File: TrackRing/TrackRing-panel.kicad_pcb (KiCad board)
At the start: 2 copper layers, 68 x 83 mm, 225 parts, among them J1 Conn_01x04, U1 TLV493D-A1B6

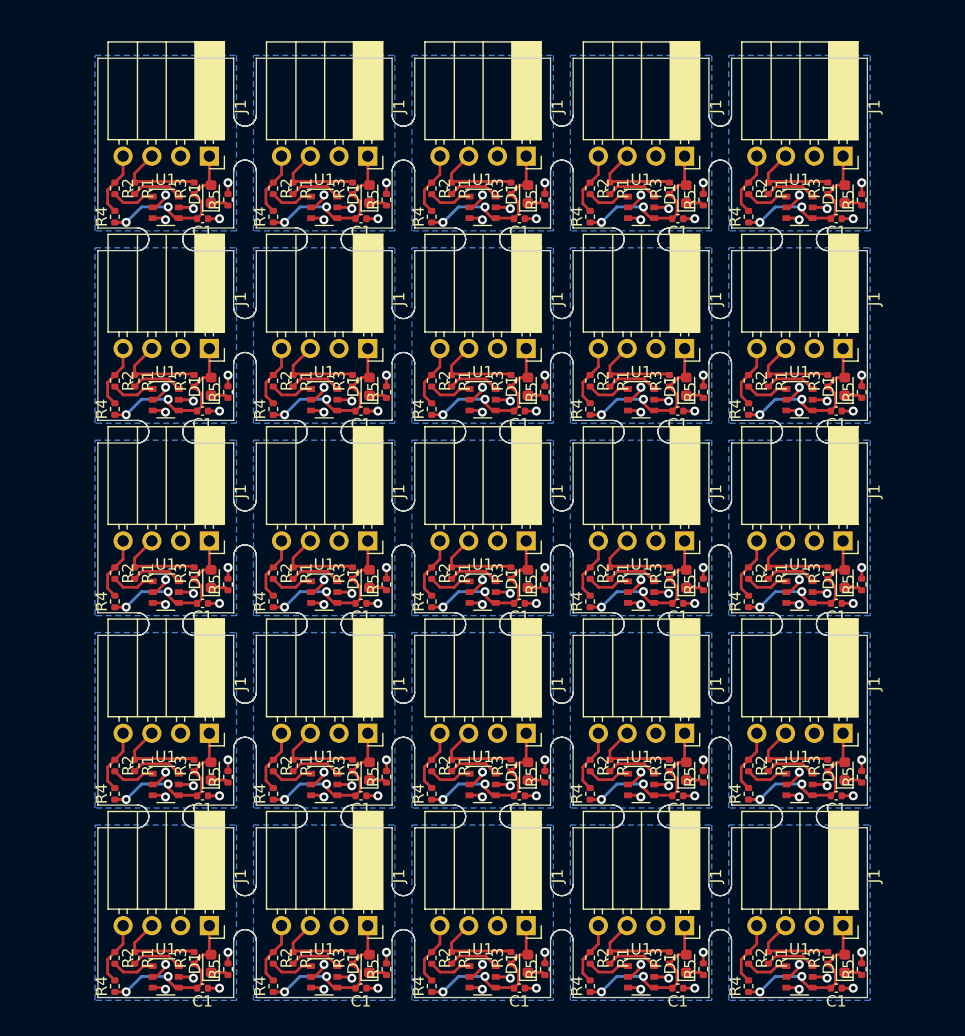
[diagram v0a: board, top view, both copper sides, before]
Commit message: Resolved various production and testing issues
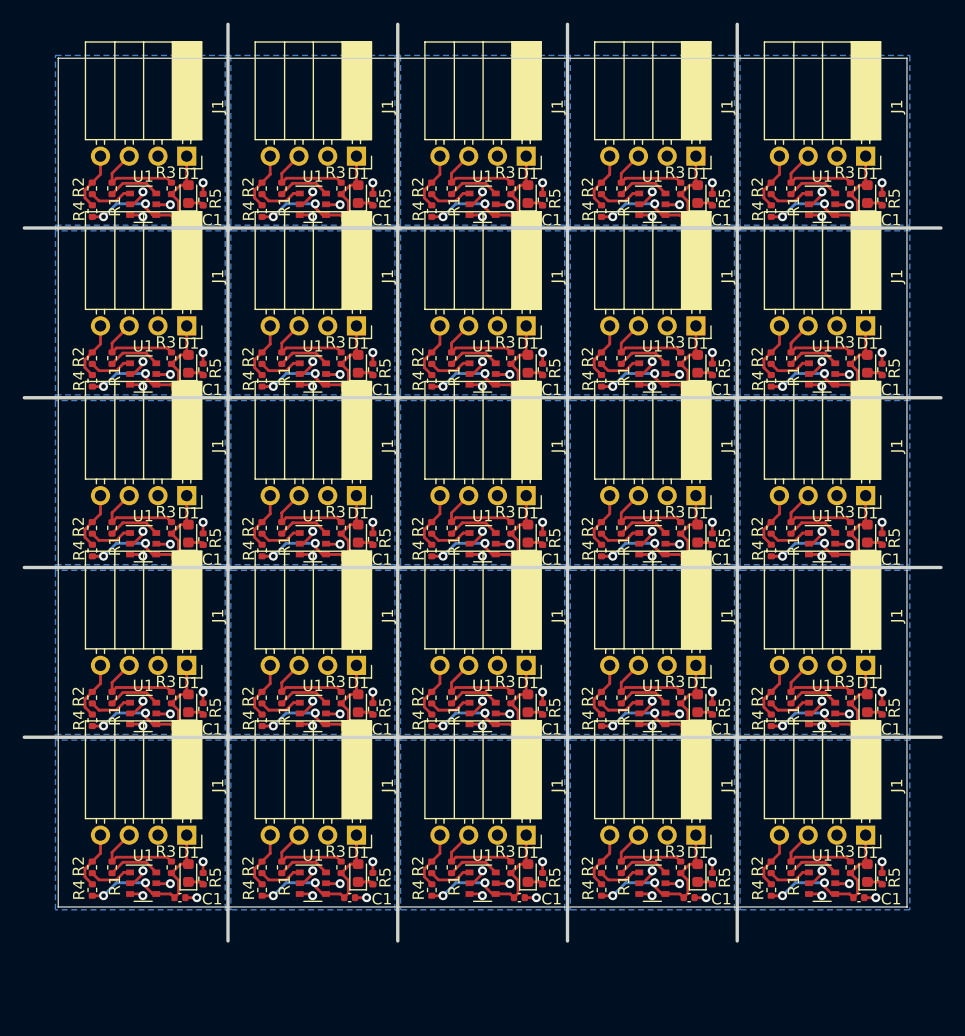
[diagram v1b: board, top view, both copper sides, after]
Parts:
- removed the C1 at (151.8, 102.2)
- removed the C1 at (179.8, 85.2)
- removed the C1 at (179.8, 34.2)
- removed the C1 at (165.8, 85.2)
- removed the C1 at (151.8, 51.2)
- removed the C1 at (123.8, 68.2)
- removed the C1 at (165.8, 102.2)
- removed the C1 at (179.8, 102.2)
- removed the C1 at (123.8, 51.2)
- removed the C1 at (151.8, 85.2)
- removed the C1 at (137.8, 51.2)
- removed the C1 at (123.8, 85.2)
- removed the C1 at (165.8, 68.2)
- removed the C1 at (165.8, 34.2)
- removed the C1 at (151.8, 34.2)
- removed the C1 at (179.8, 51.2)
- removed the C1 at (165.8, 51.2)
- removed the C1 at (179.8, 68.2)
- removed the C1 at (151.8, 68.2)
- removed the C1 at (137.8, 85.2)
- removed the C1 at (137.8, 68.2)
- removed the C1 at (137.8, 34.2)
- removed the C1 at (123.8, 102.2)
- removed the C1 at (137.8, 102.2)
- removed the D1 at (166.5, 100.0)
- removed the D1 at (180.5, 49.0)
- removed the D1 at (138.5, 49.0)
- removed the D1 at (180.5, 83.0)
- removed the D1 at (152.5, 100.0)
- removed the D1 at (166.5, 83.0)
- removed the D1 at (124.5, 66.0)
- removed the D1 at (124.5, 100.0)
- removed the D1 at (180.5, 66.0)
- removed the D1 at (138.5, 32.0)
- removed the D1 at (166.5, 49.0)
- removed the D1 at (124.5, 83.0)
- removed the D1 at (166.5, 32.0)
- removed the D1 at (138.5, 83.0)
- removed the D1 at (180.5, 32.0)
- removed the D1 at (138.5, 100.0)
- removed the D1 at (152.5, 83.0)
- removed the D1 at (138.5, 66.0)
- removed the D1 at (152.5, 66.0)
- removed the D1 at (124.5, 32.0)
- removed the D1 at (166.5, 66.0)
- removed the D1 at (152.5, 49.0)
- removed the D1 at (180.5, 100.0)
- removed the J1 at (152.3, 62.6)
- removed the J1 at (152.3, 45.6)
- removed the J1 at (124.3, 45.6)
- removed the J1 at (180.3, 45.6)
- removed the J1 at (124.3, 96.7)
- removed the J1 at (124.3, 79.7)
- removed the J1 at (138.3, 62.6)
- removed the J1 at (138.3, 96.7)
- removed the J1 at (152.3, 96.7)
- removed the J1 at (180.3, 96.7)
- removed the J1 at (124.3, 28.6)
- removed the J1 at (180.3, 79.7)
- removed the J1 at (152.3, 79.7)
- removed the J1 at (180.3, 28.6)
- removed the J1 at (166.3, 79.7)
- removed the J1 at (166.3, 96.7)
- removed the J1 at (138.3, 79.7)
- removed the J1 at (166.3, 28.6)
- removed the J1 at (180.3, 62.6)
- removed the J1 at (166.3, 45.6)
- removed the J1 at (138.3, 45.6)
- removed the J1 at (124.3, 62.6)
- removed the J1 at (166.3, 62.6)
- removed the R1 at (117.8, 99.5)
- removed the R1 at (117.8, 65.5)
- removed the R1 at (173.8, 48.5)
- removed the R1 at (131.8, 48.5)
- removed the R1 at (145.8, 48.5)
- removed the R1 at (145.8, 99.5)
- removed the R1 at (145.8, 82.5)
- removed the R1 at (131.8, 99.5)
- removed the R1 at (131.8, 65.5)
- removed the R1 at (173.8, 31.5)
- removed the R1 at (117.8, 82.5)
- removed the R1 at (131.8, 31.5)
- removed the R1 at (117.8, 48.5)
- removed the R1 at (159.8, 48.5)
- removed the R1 at (159.8, 65.5)
- removed the R1 at (173.8, 82.5)
- removed the R1 at (173.8, 99.5)
- removed the R1 at (145.8, 65.5)
- removed the R1 at (159.8, 82.5)
- removed the R1 at (159.8, 99.5)
- removed the R1 at (131.8, 82.5)
- removed the R1 at (117.8, 31.5)
- removed the R1 at (173.8, 65.5)
- removed the R2 at (172.0, 65.5)
- removed the R2 at (116.0, 48.5)
- removed the R2 at (172.0, 99.5)
- removed the R2 at (130.0, 65.5)
- removed the R2 at (116.0, 65.5)
- removed the R2 at (144.0, 48.5)
- removed the R2 at (144.0, 82.5)
- removed the R2 at (172.0, 48.5)
- removed the R2 at (130.0, 31.5)
- removed the R2 at (130.0, 82.5)
- removed the R2 at (158.0, 99.5)
- removed the R2 at (158.0, 31.5)
- removed the R2 at (172.0, 82.5)
- removed the R2 at (144.0, 99.5)
- removed the R2 at (130.0, 99.5)
- removed the R2 at (130.0, 48.5)
- removed the R2 at (158.0, 48.5)
- removed the R2 at (158.0, 65.5)
- removed the R2 at (116.0, 99.5)
- removed the R2 at (158.0, 82.5)
- removed the R2 at (144.0, 65.5)
- removed the R2 at (116.0, 82.5)
- removed the R2 at (172.0, 31.5)
- removed the R3 at (151.0, 48.5)
- removed the R3 at (151.0, 82.5)
- removed the R3 at (123.0, 48.5)
- removed the R3 at (151.0, 99.5)
- removed the R3 at (137.0, 65.5)
- removed the R3 at (137.0, 48.5)
- removed the R3 at (137.0, 99.5)
- removed the R3 at (123.0, 31.5)
- removed the R3 at (165.0, 65.5)
- removed the R3 at (165.0, 82.5)
- removed the R3 at (123.0, 99.5)
- removed the R3 at (165.0, 48.5)
- removed the R3 at (179.0, 48.5)
- removed the R3 at (179.0, 65.5)
- removed the R3 at (165.0, 99.5)
- removed the R3 at (137.0, 82.5)
- removed the R3 at (179.0, 99.5)
- removed the R3 at (123.0, 65.5)
- removed the R3 at (151.0, 65.5)
- removed the R3 at (137.0, 31.5)
- removed the R3 at (179.0, 82.5)
- removed the R3 at (123.0, 82.5)
- removed the R3 at (165.0, 31.5)
- removed the R4 at (144.0, 68.0)
- removed the R4 at (172.0, 102.0)
- removed the R4 at (130.0, 102.0)
- removed the R4 at (172.0, 34.0)
- removed the R4 at (130.0, 51.0)
- removed the R4 at (158.0, 51.0)
- removed the R4 at (116.0, 51.0)
- removed the R4 at (158.0, 102.0)
- removed the R4 at (116.0, 102.0)
- removed the R4 at (144.0, 85.0)
- removed the R4 at (144.0, 51.0)
- removed the R4 at (172.0, 68.0)
- removed the R4 at (144.0, 102.0)
- removed the R4 at (158.0, 68.0)
- removed the R4 at (144.0, 34.0)
- removed the R4 at (158.0, 34.0)
- removed the R4 at (158.0, 85.0)
- removed the R4 at (116.0, 34.0)
- removed the R4 at (130.0, 68.0)
- removed the R4 at (116.0, 85.0)
- removed the R4 at (116.0, 68.0)
- removed the R4 at (172.0, 51.0)
- removed the R4 at (172.0, 85.0)
- removed the R4 at (130.0, 85.0)
- removed the R5 at (154.0, 66.5)
- removed the R5 at (140.0, 83.5)
- removed the R5 at (126.0, 83.5)
- removed the R5 at (182.0, 32.5)
- removed the R5 at (154.0, 100.5)
- removed the R5 at (182.0, 49.5)
- removed the R5 at (154.0, 32.5)
- removed the R5 at (168.0, 66.5)
- removed the R5 at (154.0, 49.5)
- removed the R5 at (126.0, 100.5)
- removed the R5 at (182.0, 83.5)
- removed the R5 at (168.0, 49.5)
- removed the R5 at (154.0, 83.5)
- removed the R5 at (140.0, 49.5)
- removed the R5 at (126.0, 49.5)
- removed the R5 at (126.0, 66.5)
- removed the R5 at (140.0, 100.5)
- removed the R5 at (182.0, 100.5)
- removed the R5 at (126.0, 32.5)
- removed the R5 at (168.0, 100.5)
- removed the R5 at (168.0, 83.5)
- removed the R5 at (168.0, 32.5)
- removed the R5 at (182.0, 66.5)
- removed the R5 at (140.0, 66.5)
- removed the U1 at (162.5, 50.2)
- removed the U1 at (176.5, 67.2)
- removed the U1 at (148.5, 84.2)
- removed the U1 at (176.5, 101.2)
- removed the U1 at (120.5, 84.2)
- removed the U1 at (176.5, 50.2)
- removed the U1 at (120.5, 33.2)
- removed the U1 at (120.5, 50.2)
- removed the U1 at (134.5, 50.2)
- removed the U1 at (176.5, 84.2)
- removed the U1 at (162.5, 67.2)
- removed the U1 at (134.5, 67.2)
- removed the U1 at (148.5, 50.2)
- removed the U1 at (134.5, 84.2)
- removed the U1 at (176.5, 33.2)
- removed the U1 at (134.5, 101.2)
- removed the U1 at (148.5, 33.2)
- removed the U1 at (148.5, 101.2)
- removed the U1 at (120.5, 67.2)
- removed the U1 at (148.5, 67.2)
- removed the U1 at (162.5, 33.2)
- removed the U1 at (134.5, 33.2)
- removed the U1 at (120.5, 101.2)
- removed the U1 at (162.5, 101.2)
- added C1: 0.1uF, Capacitor_SMD:C_0402_1005Metric, F.Cu at (136.8, 94.2)
- added C1: 0.1uF, Capacitor_SMD:C_0402_1005Metric, F.Cu at (166.8, 79.2)
- added C1: 0.1uF, Capacitor_SMD:C_0402_1005Metric, F.Cu at (136.8, 64.2)
- added C1: 0.1uF, Capacitor_SMD:C_0402_1005Metric, F.Cu at (136.8, 79.2)
- added C1: 0.1uF, Capacitor_SMD:C_0402_1005Metric, F.Cu at (121.8, 79.2)
- added C1: 0.1uF, Capacitor_SMD:C_0402_1005Metric, F.Cu at (166.8, 94.2)
- added C1: 0.1uF, Capacitor_SMD:C_0402_1005Metric, F.Cu at (151.8, 94.2)
- added C1: 0.1uF, Capacitor_SMD:C_0402_1005Metric, F.Cu at (121.8, 49.2)
- added C1: 0.1uF, Capacitor_SMD:C_0402_1005Metric, F.Cu at (166.8, 49.2)
- added C1: 0.1uF, Capacitor_SMD:C_0402_1005Metric, F.Cu at (121.8, 34.2)
- added C1: 0.1uF, Capacitor_SMD:C_0402_1005Metric, F.Cu at (181.8, 94.2)
- added C1: 0.1uF, Capacitor_SMD:C_0402_1005Metric, F.Cu at (151.8, 64.2)
- added C1: 0.1uF, Capacitor_SMD:C_0402_1005Metric, F.Cu at (136.8, 34.2)
- added C1: 0.1uF, Capacitor_SMD:C_0402_1005Metric, F.Cu at (121.8, 94.2)
- added C1: 0.1uF, Capacitor_SMD:C_0402_1005Metric, F.Cu at (181.8, 49.2)
- added C1: 0.1uF, Capacitor_SMD:C_0402_1005Metric, F.Cu at (166.8, 34.2)
- added C1: 0.1uF, Capacitor_SMD:C_0402_1005Metric, F.Cu at (181.8, 34.2)
- added C1: 0.1uF, Capacitor_SMD:C_0402_1005Metric, F.Cu at (166.8, 64.2)
- added C1: 0.1uF, Capacitor_SMD:C_0402_1005Metric, F.Cu at (181.8, 79.2)
- added C1: 0.1uF, Capacitor_SMD:C_0402_1005Metric, F.Cu at (151.8, 79.2)
- added C1: 0.1uF, Capacitor_SMD:C_0402_1005Metric, F.Cu at (121.8, 64.2)
- added C1: 0.1uF, Capacitor_SMD:C_0402_1005Metric, F.Cu at (151.8, 49.2)
- added C1: 0.1uF, Capacitor_SMD:C_0402_1005Metric, F.Cu at (181.8, 64.2)
- added C1: 0.1uF, Capacitor_SMD:C_0402_1005Metric, F.Cu at (136.8, 49.2)
- added D1: LED, LED_SMD:LED_0603_1608Metric, F.Cu at (122.5, 77.0)
- added D1: LED, LED_SMD:LED_0603_1608Metric, F.Cu at (137.5, 77.0)
- added D1: LED, LED_SMD:LED_0603_1608Metric, F.Cu at (167.5, 47.0)
- added D1: LED, LED_SMD:LED_0603_1608Metric, F.Cu at (122.5, 62.0)
- added D1: LED, LED_SMD:LED_0603_1608Metric, F.Cu at (152.5, 77.0)
- added D1: LED, LED_SMD:LED_0603_1608Metric, F.Cu at (137.5, 32.0)
- added D1: LED, LED_SMD:LED_0603_1608Metric, F.Cu at (167.5, 62.0)
- added D1: LED, LED_SMD:LED_0603_1608Metric, F.Cu at (152.5, 62.0)
- added D1: LED, LED_SMD:LED_0603_1608Metric, F.Cu at (182.5, 32.0)
- added D1: LED, LED_SMD:LED_0603_1608Metric, F.Cu at (152.5, 92.0)
- added D1: LED, LED_SMD:LED_0603_1608Metric, F.Cu at (137.5, 47.0)
- added D1: LED, LED_SMD:LED_0603_1608Metric, F.Cu at (182.5, 77.0)
- added D1: LED, LED_SMD:LED_0603_1608Metric, F.Cu at (137.5, 92.0)
- added D1: LED, LED_SMD:LED_0603_1608Metric, F.Cu at (122.5, 32.0)
- added D1: LED, LED_SMD:LED_0603_1608Metric, F.Cu at (182.5, 62.0)
- added D1: LED, LED_SMD:LED_0603_1608Metric, F.Cu at (182.5, 92.0)
- added D1: LED, LED_SMD:LED_0603_1608Metric, F.Cu at (137.5, 62.0)
- added D1: LED, LED_SMD:LED_0603_1608Metric, F.Cu at (152.5, 47.0)
- added D1: LED, LED_SMD:LED_0603_1608Metric, F.Cu at (167.5, 77.0)
- added D1: LED, LED_SMD:LED_0603_1608Metric, F.Cu at (167.5, 92.0)
- added D1: LED, LED_SMD:LED_0603_1608Metric, F.Cu at (167.5, 32.0)
- added D1: LED, LED_SMD:LED_0603_1608Metric, F.Cu at (122.5, 47.0)
- added D1: LED, LED_SMD:LED_0603_1608Metric, F.Cu at (182.5, 47.0)
- added J1: Conn_01x04, Connector_PinSocket_2.54mm:PinSocket_1x04_P2.54mm_Horizontal, F.Cu at (152.3, 43.6)
- added J1: Conn_01x04, Connector_PinSocket_2.54mm:PinSocket_1x04_P2.54mm_Horizontal, F.Cu at (167.3, 88.7)
- added J1: Conn_01x04, Connector_PinSocket_2.54mm:PinSocket_1x04_P2.54mm_Horizontal, F.Cu at (137.3, 43.6)
- added J1: Conn_01x04, Connector_PinSocket_2.54mm:PinSocket_1x04_P2.54mm_Horizontal, F.Cu at (167.3, 28.6)
- added J1: Conn_01x04, Connector_PinSocket_2.54mm:PinSocket_1x04_P2.54mm_Horizontal, F.Cu at (182.3, 88.7)
- added J1: Conn_01x04, Connector_PinSocket_2.54mm:PinSocket_1x04_P2.54mm_Horizontal, F.Cu at (152.3, 58.6)
- added J1: Conn_01x04, Connector_PinSocket_2.54mm:PinSocket_1x04_P2.54mm_Horizontal, F.Cu at (122.3, 43.6)
- added J1: Conn_01x04, Connector_PinSocket_2.54mm:PinSocket_1x04_P2.54mm_Horizontal, F.Cu at (122.3, 88.7)
- added J1: Conn_01x04, Connector_PinSocket_2.54mm:PinSocket_1x04_P2.54mm_Horizontal, F.Cu at (152.3, 88.7)
- added J1: Conn_01x04, Connector_PinSocket_2.54mm:PinSocket_1x04_P2.54mm_Horizontal, F.Cu at (137.3, 88.7)
- added J1: Conn_01x04, Connector_PinSocket_2.54mm:PinSocket_1x04_P2.54mm_Horizontal, F.Cu at (137.3, 73.7)
- added J1: Conn_01x04, Connector_PinSocket_2.54mm:PinSocket_1x04_P2.54mm_Horizontal, F.Cu at (122.3, 28.6)
- added J1: Conn_01x04, Connector_PinSocket_2.54mm:PinSocket_1x04_P2.54mm_Horizontal, F.Cu at (167.3, 43.6)
- added J1: Conn_01x04, Connector_PinSocket_2.54mm:PinSocket_1x04_P2.54mm_Horizontal, F.Cu at (182.3, 73.7)
- added J1: Conn_01x04, Connector_PinSocket_2.54mm:PinSocket_1x04_P2.54mm_Horizontal, F.Cu at (167.3, 58.6)
- added J1: Conn_01x04, Connector_PinSocket_2.54mm:PinSocket_1x04_P2.54mm_Horizontal, F.Cu at (122.3, 58.6)
- added J1: Conn_01x04, Connector_PinSocket_2.54mm:PinSocket_1x04_P2.54mm_Horizontal, F.Cu at (182.3, 28.6)
- added J1: Conn_01x04, Connector_PinSocket_2.54mm:PinSocket_1x04_P2.54mm_Horizontal, F.Cu at (182.3, 43.6)
- added J1: Conn_01x04, Connector_PinSocket_2.54mm:PinSocket_1x04_P2.54mm_Horizontal, F.Cu at (152.3, 73.7)
- added J1: Conn_01x04, Connector_PinSocket_2.54mm:PinSocket_1x04_P2.54mm_Horizontal, F.Cu at (182.3, 58.6)
- added J1: Conn_01x04, Connector_PinSocket_2.54mm:PinSocket_1x04_P2.54mm_Horizontal, F.Cu at (122.3, 73.7)
- added J1: Conn_01x04, Connector_PinSocket_2.54mm:PinSocket_1x04_P2.54mm_Horizontal, F.Cu at (137.3, 58.6)
- added J1: Conn_01x04, Connector_PinSocket_2.54mm:PinSocket_1x04_P2.54mm_Horizontal, F.Cu at (167.3, 73.7)
- added R1: 100, Resistor_SMD:R_0402_1005Metric, F.Cu at (115.8, 91.5)
- added R1: 100, Resistor_SMD:R_0402_1005Metric, F.Cu at (160.8, 46.5)
- added R1: 100, Resistor_SMD:R_0402_1005Metric, F.Cu at (145.8, 46.5)
- added R1: 100, Resistor_SMD:R_0402_1005Metric, F.Cu at (115.8, 31.5)
- added R1: 100, Resistor_SMD:R_0402_1005Metric, F.Cu at (130.8, 76.5)
- added R1: 100, Resistor_SMD:R_0402_1005Metric, F.Cu at (160.8, 91.5)
- added R1: 100, Resistor_SMD:R_0402_1005Metric, F.Cu at (115.8, 46.5)
- added R1: 100, Resistor_SMD:R_0402_1005Metric, F.Cu at (175.8, 91.5)
- added R1: 100, Resistor_SMD:R_0402_1005Metric, F.Cu at (130.8, 46.5)
- added R1: 100, Resistor_SMD:R_0402_1005Metric, F.Cu at (175.8, 31.5)
- added R1: 100, Resistor_SMD:R_0402_1005Metric, F.Cu at (115.8, 61.5)
- added R1: 100, Resistor_SMD:R_0402_1005Metric, F.Cu at (115.8, 76.5)
- added R1: 100, Resistor_SMD:R_0402_1005Metric, F.Cu at (160.8, 61.5)
- added R1: 100, Resistor_SMD:R_0402_1005Metric, F.Cu at (160.8, 76.5)
- added R1: 100, Resistor_SMD:R_0402_1005Metric, F.Cu at (130.8, 31.5)
- added R1: 100, Resistor_SMD:R_0402_1005Metric, F.Cu at (145.8, 76.5)
- added R1: 100, Resistor_SMD:R_0402_1005Metric, F.Cu at (175.8, 46.5)
- added R1: 100, Resistor_SMD:R_0402_1005Metric, F.Cu at (130.8, 61.5)
- added R1: 100, Resistor_SMD:R_0402_1005Metric, F.Cu at (175.8, 76.5)
- added R1: 100, Resistor_SMD:R_0402_1005Metric, F.Cu at (160.8, 31.5)
- added R1: 100, Resistor_SMD:R_0402_1005Metric, F.Cu at (145.8, 91.5)
- added R1: 100, Resistor_SMD:R_0402_1005Metric, F.Cu at (175.8, 61.5)
- added R1: 100, Resistor_SMD:R_0402_1005Metric, F.Cu at (130.8, 91.5)
- added R2: 100, Resistor_SMD:R_0402_1005Metric, F.Cu at (174.0, 61.5)
- added R2: 100, Resistor_SMD:R_0402_1005Metric, F.Cu at (129.0, 91.5)
- added R2: 100, Resistor_SMD:R_0402_1005Metric, F.Cu at (174.0, 91.5)
- added R2: 100, Resistor_SMD:R_0402_1005Metric, F.Cu at (114.0, 76.5)
- added R2: 100, Resistor_SMD:R_0402_1005Metric, F.Cu at (174.0, 76.5)
- added R2: 100, Resistor_SMD:R_0402_1005Metric, F.Cu at (129.0, 76.5)
- added R2: 100, Resistor_SMD:R_0402_1005Metric, F.Cu at (159.0, 46.5)
- added R2: 100, Resistor_SMD:R_0402_1005Metric, F.Cu at (144.0, 61.5)
- added R2: 100, Resistor_SMD:R_0402_1005Metric, F.Cu at (114.0, 61.5)
- added R2: 100, Resistor_SMD:R_0402_1005Metric, F.Cu at (129.0, 61.5)
- added R2: 100, Resistor_SMD:R_0402_1005Metric, F.Cu at (159.0, 76.5)
- added R2: 100, Resistor_SMD:R_0402_1005Metric, F.Cu at (144.0, 46.5)
- added R2: 100, Resistor_SMD:R_0402_1005Metric, F.Cu at (144.0, 76.5)
- added R2: 100, Resistor_SMD:R_0402_1005Metric, F.Cu at (159.0, 31.5)
- added R2: 100, Resistor_SMD:R_0402_1005Metric, F.Cu at (159.0, 91.5)
- added R2: 100, Resistor_SMD:R_0402_1005Metric, F.Cu at (159.0, 61.5)
- added R2: 100, Resistor_SMD:R_0402_1005Metric, F.Cu at (144.0, 91.5)
- added R2: 100, Resistor_SMD:R_0402_1005Metric, F.Cu at (114.0, 31.5)
- added R2: 100, Resistor_SMD:R_0402_1005Metric, F.Cu at (114.0, 91.5)
- added R2: 100, Resistor_SMD:R_0402_1005Metric, F.Cu at (129.0, 31.5)
- added R2: 100, Resistor_SMD:R_0402_1005Metric, F.Cu at (129.0, 46.5)
- added R2: 100, Resistor_SMD:R_0402_1005Metric, F.Cu at (174.0, 31.5)
- added R2: 100, Resistor_SMD:R_0402_1005Metric, F.Cu at (174.0, 46.5)
- added R3: 1.2K, Resistor_SMD:R_0402_1005Metric, F.Cu at (181.0, 76.5)
- added R3: 1.2K, Resistor_SMD:R_0402_1005Metric, F.Cu at (151.0, 46.5)
- added R3: 1.2K, Resistor_SMD:R_0402_1005Metric, F.Cu at (121.0, 91.5)
- added R3: 1.2K, Resistor_SMD:R_0402_1005Metric, F.Cu at (181.0, 61.5)
- added R3: 1.2K, Resistor_SMD:R_0402_1005Metric, F.Cu at (166.0, 31.5)
- added R3: 1.2K, Resistor_SMD:R_0402_1005Metric, F.Cu at (121.0, 46.5)
- added R3: 1.2K, Resistor_SMD:R_0402_1005Metric, F.Cu at (181.0, 91.5)
- added R3: 1.2K, Resistor_SMD:R_0402_1005Metric, F.Cu at (121.0, 31.5)
- added R3: 1.2K, Resistor_SMD:R_0402_1005Metric, F.Cu at (136.0, 76.5)
- added R3: 1.2K, Resistor_SMD:R_0402_1005Metric, F.Cu at (121.0, 61.5)
- added R3: 1.2K, Resistor_SMD:R_0402_1005Metric, F.Cu at (151.0, 91.5)
- added R3: 1.2K, Resistor_SMD:R_0402_1005Metric, F.Cu at (136.0, 31.5)
- added R3: 1.2K, Resistor_SMD:R_0402_1005Metric, F.Cu at (121.0, 76.5)
- added R3: 1.2K, Resistor_SMD:R_0402_1005Metric, F.Cu at (181.0, 46.5)
- added R3: 1.2K, Resistor_SMD:R_0402_1005Metric, F.Cu at (151.0, 76.5)
- added R3: 1.2K, Resistor_SMD:R_0402_1005Metric, F.Cu at (136.0, 61.5)
- added R3: 1.2K, Resistor_SMD:R_0402_1005Metric, F.Cu at (151.0, 61.5)
- added R3: 1.2K, Resistor_SMD:R_0402_1005Metric, F.Cu at (166.0, 61.5)
- added R3: 1.2K, Resistor_SMD:R_0402_1005Metric, F.Cu at (166.0, 76.5)
- added R3: 1.2K, Resistor_SMD:R_0402_1005Metric, F.Cu at (166.0, 91.5)
- added R3: 1.2K, Resistor_SMD:R_0402_1005Metric, F.Cu at (136.0, 91.5)
- added R3: 1.2K, Resistor_SMD:R_0402_1005Metric, F.Cu at (166.0, 46.5)
- added R3: 1.2K, Resistor_SMD:R_0402_1005Metric, F.Cu at (136.0, 46.5)
- added R4: 1.2K, Resistor_SMD:R_0402_1005Metric, F.Cu at (129.0, 78.5)
- added R4: 1.2K, Resistor_SMD:R_0402_1005Metric, F.Cu at (159.0, 93.5)
- added R4: 1.2K, Resistor_SMD:R_0402_1005Metric, F.Cu at (174.0, 63.5)
- added R4: 1.2K, Resistor_SMD:R_0402_1005Metric, F.Cu at (129.0, 33.5)
- added R4: 1.2K, Resistor_SMD:R_0402_1005Metric, F.Cu at (144.0, 93.5)
- added R4: 1.2K, Resistor_SMD:R_0402_1005Metric, F.Cu at (159.0, 63.5)
- added R4: 1.2K, Resistor_SMD:R_0402_1005Metric, F.Cu at (129.0, 93.5)
- added R4: 1.2K, Resistor_SMD:R_0402_1005Metric, F.Cu at (114.0, 33.5)
- added R4: 1.2K, Resistor_SMD:R_0402_1005Metric, F.Cu at (114.0, 93.5)
- added R4: 1.2K, Resistor_SMD:R_0402_1005Metric, F.Cu at (144.0, 33.5)
- added R4: 1.2K, Resistor_SMD:R_0402_1005Metric, F.Cu at (114.0, 63.5)
- added R4: 1.2K, Resistor_SMD:R_0402_1005Metric, F.Cu at (159.0, 48.5)
- added R4: 1.2K, Resistor_SMD:R_0402_1005Metric, F.Cu at (129.0, 63.5)
- added R4: 1.2K, Resistor_SMD:R_0402_1005Metric, F.Cu at (144.0, 63.5)
- added R4: 1.2K, Resistor_SMD:R_0402_1005Metric, F.Cu at (174.0, 78.5)
- added R4: 1.2K, Resistor_SMD:R_0402_1005Metric, F.Cu at (174.0, 33.5)
- added R4: 1.2K, Resistor_SMD:R_0402_1005Metric, F.Cu at (114.0, 48.5)
- added R4: 1.2K, Resistor_SMD:R_0402_1005Metric, F.Cu at (174.0, 93.5)
- added R4: 1.2K, Resistor_SMD:R_0402_1005Metric, F.Cu at (114.0, 78.5)
- added R4: 1.2K, Resistor_SMD:R_0402_1005Metric, F.Cu at (129.0, 48.5)
- added R4: 1.2K, Resistor_SMD:R_0402_1005Metric, F.Cu at (144.0, 48.5)
- added R4: 1.2K, Resistor_SMD:R_0402_1005Metric, F.Cu at (174.0, 48.5)
- added R4: 1.2K, Resistor_SMD:R_0402_1005Metric, F.Cu at (144.0, 78.5)
- added R4: 1.2K, Resistor_SMD:R_0402_1005Metric, F.Cu at (159.0, 78.5)
- added R5: 500, Resistor_SMD:R_0402_1005Metric, F.Cu at (123.8, 92.5)
- added R5: 500, Resistor_SMD:R_0402_1005Metric, F.Cu at (183.8, 47.5)
- added R5: 500, Resistor_SMD:R_0402_1005Metric, F.Cu at (153.8, 47.5)
- added R5: 500, Resistor_SMD:R_0402_1005Metric, F.Cu at (138.8, 77.5)
- added R5: 500, Resistor_SMD:R_0402_1005Metric, F.Cu at (153.8, 77.5)
- added R5: 500, Resistor_SMD:R_0402_1005Metric, F.Cu at (183.8, 62.5)
- added R5: 500, Resistor_SMD:R_0402_1005Metric, F.Cu at (183.8, 32.5)
- added R5: 500, Resistor_SMD:R_0402_1005Metric, F.Cu at (168.8, 92.5)
- added R5: 500, Resistor_SMD:R_0402_1005Metric, F.Cu at (123.8, 32.5)
- added R5: 500, Resistor_SMD:R_0402_1005Metric, F.Cu at (138.8, 92.5)
- added R5: 500, Resistor_SMD:R_0402_1005Metric, F.Cu at (123.8, 47.5)
- added R5: 500, Resistor_SMD:R_0402_1005Metric, F.Cu at (153.8, 32.5)
- added R5: 500, Resistor_SMD:R_0402_1005Metric, F.Cu at (183.8, 92.5)
- added R5: 500, Resistor_SMD:R_0402_1005Metric, F.Cu at (168.8, 32.5)
- added R5: 500, Resistor_SMD:R_0402_1005Metric, F.Cu at (123.8, 77.5)
- added R5: 500, Resistor_SMD:R_0402_1005Metric, F.Cu at (153.8, 92.5)
- added R5: 500, Resistor_SMD:R_0402_1005Metric, F.Cu at (138.8, 62.5)
- added R5: 500, Resistor_SMD:R_0402_1005Metric, F.Cu at (138.8, 47.5)
- added R5: 500, Resistor_SMD:R_0402_1005Metric, F.Cu at (123.8, 62.5)
- added R5: 500, Resistor_SMD:R_0402_1005Metric, F.Cu at (168.8, 47.5)
- added R5: 500, Resistor_SMD:R_0402_1005Metric, F.Cu at (183.8, 77.5)
- added R5: 500, Resistor_SMD:R_0402_1005Metric, F.Cu at (168.8, 77.5)
- added R5: 500, Resistor_SMD:R_0402_1005Metric, F.Cu at (168.8, 62.5)
- added R5: 500, Resistor_SMD:R_0402_1005Metric, F.Cu at (153.8, 62.5)
- added U1: TLV493D-A1B6, Package_SO:TSOP-6_1.65x3.05mm_P0.95mm, F.Cu at (148.5, 47.9)
- added U1: TLV493D-A1B6, Package_SO:TSOP-6_1.65x3.05mm_P0.95mm, F.Cu at (178.5, 77.9)
- added U1: TLV493D-A1B6, Package_SO:TSOP-6_1.65x3.05mm_P0.95mm, F.Cu at (178.5, 32.9)
- added U1: TLV493D-A1B6, Package_SO:TSOP-6_1.65x3.05mm_P0.95mm, F.Cu at (148.5, 62.9)
- added U1: TLV493D-A1B6, Package_SO:TSOP-6_1.65x3.05mm_P0.95mm, F.Cu at (178.5, 62.9)
- added U1: TLV493D-A1B6, Package_SO:TSOP-6_1.65x3.05mm_P0.95mm, F.Cu at (148.5, 32.9)
- added U1: TLV493D-A1B6, Package_SO:TSOP-6_1.65x3.05mm_P0.95mm, F.Cu at (118.5, 32.9)
- added U1: TLV493D-A1B6, Package_SO:TSOP-6_1.65x3.05mm_P0.95mm, F.Cu at (178.5, 92.9)
- added U1: TLV493D-A1B6, Package_SO:TSOP-6_1.65x3.05mm_P0.95mm, F.Cu at (118.5, 92.9)
- added U1: TLV493D-A1B6, Package_SO:TSOP-6_1.65x3.05mm_P0.95mm, F.Cu at (148.5, 77.9)
- added U1: TLV493D-A1B6, Package_SO:TSOP-6_1.65x3.05mm_P0.95mm, F.Cu at (118.5, 77.9)
- added U1: TLV493D-A1B6, Package_SO:TSOP-6_1.65x3.05mm_P0.95mm, F.Cu at (148.5, 92.9)
- added U1: TLV493D-A1B6, Package_SO:TSOP-6_1.65x3.05mm_P0.95mm, F.Cu at (133.5, 47.9)
- added U1: TLV493D-A1B6, Package_SO:TSOP-6_1.65x3.05mm_P0.95mm, F.Cu at (163.5, 92.9)
- added U1: TLV493D-A1B6, Package_SO:TSOP-6_1.65x3.05mm_P0.95mm, F.Cu at (163.5, 77.9)
- added U1: TLV493D-A1B6, Package_SO:TSOP-6_1.65x3.05mm_P0.95mm, F.Cu at (178.5, 47.9)
- added U1: TLV493D-A1B6, Package_SO:TSOP-6_1.65x3.05mm_P0.95mm, F.Cu at (118.5, 62.9)
- added U1: TLV493D-A1B6, Package_SO:TSOP-6_1.65x3.05mm_P0.95mm, F.Cu at (133.5, 62.9)
- added U1: TLV493D-A1B6, Package_SO:TSOP-6_1.65x3.05mm_P0.95mm, F.Cu at (118.5, 47.9)
- added U1: TLV493D-A1B6, Package_SO:TSOP-6_1.65x3.05mm_P0.95mm, F.Cu at (133.5, 77.9)
- added U1: TLV493D-A1B6, Package_SO:TSOP-6_1.65x3.05mm_P0.95mm, F.Cu at (163.5, 62.9)
- added U1: TLV493D-A1B6, Package_SO:TSOP-6_1.65x3.05mm_P0.95mm, F.Cu at (163.5, 32.9)
- added U1: TLV493D-A1B6, Package_SO:TSOP-6_1.65x3.05mm_P0.95mm, F.Cu at (163.5, 47.9)
- added U1: TLV493D-A1B6, Package_SO:TSOP-6_1.65x3.05mm_P0.95mm, F.Cu at (133.5, 92.9)
- moved U1 58.9 mm to (133.5, 32.9)
- moved D1 43.0 mm to (122.5, 92.0)
- moved R1 33.1 mm to (145.8, 61.5)
- moved R4 29.0 mm to (159.0, 33.5)
- moved C1 28.0 mm to (151.8, 34.2)
- moved R2 15.1 mm to (114.0, 46.5)
- moved R3 2.00 mm to (181.0, 31.5)
- moved R5 1.20 mm to (138.8, 32.5)
- moved J1 1.00 mm to (137.3, 28.6)
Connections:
- C1 pad 1: Board_0-GND -> Board_2-GND
- C1 pad 2: Board_0-/VCC -> Board_2-/VCC
- D1 pad 1: Board_5-Net-(D1-K) -> Board_20-Net-(D1-K)
- D1 pad 2: Board_5-/VCC -> Board_20-/VCC
- R1 pad 1: Board_3-/SDA -> Board_12-/SDA
- R1 pad 2: Board_3-Net-(U1-SDA) -> Board_12-Net-(U1-SDA)
- R2 pad 1: Board_0-/SCL -> Board_5-/SCL
- R2 pad 2: Board_0-Net-(U1-SCL) -> Board_5-Net-(U1-SCL)
- R4 pad 1: Board_1-/VCC -> Board_3-/VCC
- R4 pad 2: Board_1-/SCL -> Board_3-/SCL
- U1 pad 1: Board_18-Net-(U1-SCL) -> Board_1-Net-(U1-SCL)
- U1 pad 2: Board_18-GND -> Board_1-GND
- U1 pad 3: Board_18-GND -> Board_1-GND
- U1 pad 4: Board_18-/VCC -> Board_1-/VCC
- U1 pad 5: Board_18-GND -> Board_1-GND
- U1 pad 6: Board_18-Net-(U1-SDA) -> Board_1-Net-(U1-SDA)
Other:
- board size 68 x 83 mm -> 81 x 81 mm
